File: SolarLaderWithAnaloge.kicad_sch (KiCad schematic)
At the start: 31 parts, among them J1 Conn_01x04, J2 Conn_01x02, J3 Conn_01x01, J4 UKDBBTAAA, J5 Conn_01x02, Q1 AO3401A, U1 BQ25185DLHR, U2 LM66200DRLR

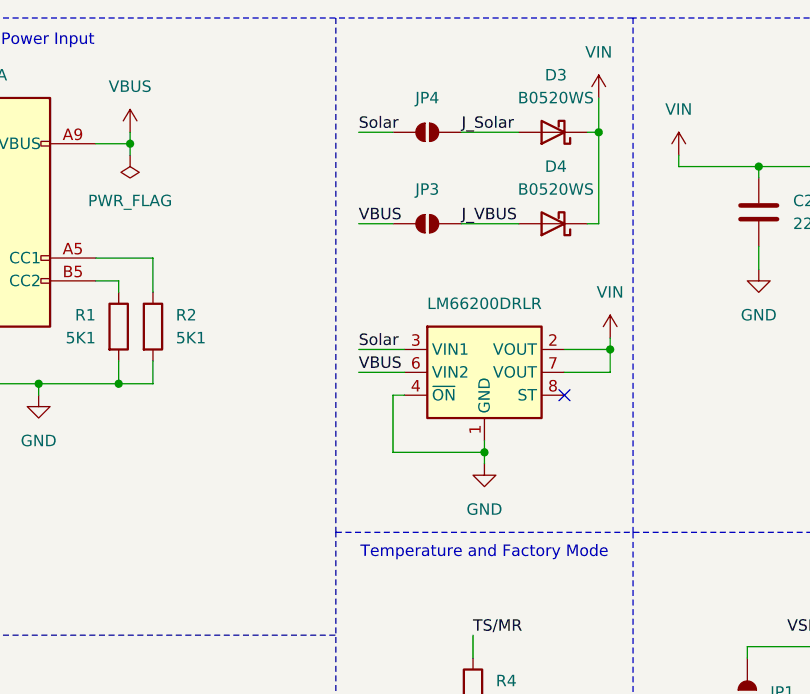
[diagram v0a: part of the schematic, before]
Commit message: Update the Jumper for the input
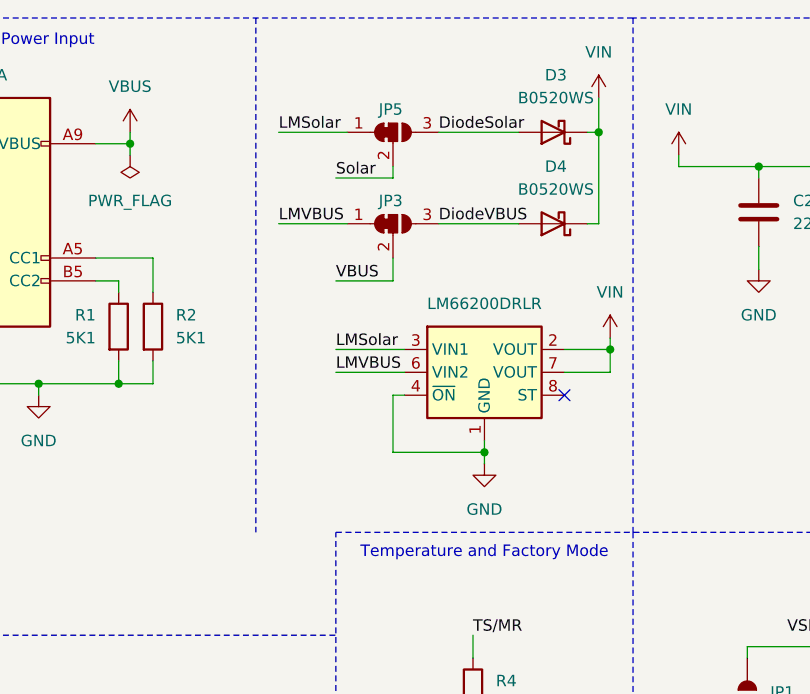
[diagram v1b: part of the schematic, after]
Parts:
- removed JP3, JP4: SolderJumper_2_Open, Jumper:SolderJumper-2_P1.3mm_Open_Pad1.0x1.5mm, symbol Jumper:SolderJumper_2_Open
- added JP3, JP5: SolderJumper_3_Bridged12, Jumper:SolderJumper-3_P1.3mm_Bridged12_Pad1.0x1.5mm, symbol Jumper:SolderJumper_3_Bridged12
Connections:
- net Solar: now also JP5.2 (C); no longer U2.3 (VIN1)
- net VBUS: now also JP3.2 (C); no longer U2.6 (VIN2)
- net J_Solar renamed DiodeSolar
- net DiodeSolar: now also JP5.3 (B)
- net J_VBUS renamed DiodeVBUS
- net DiodeVBUS: now also JP3.3 (B)
- new net LMSolar: JP5.1 (A), U2.3 (VIN1)
- new net LMVBUS: JP3.1 (A), U2.6 (VIN2)
